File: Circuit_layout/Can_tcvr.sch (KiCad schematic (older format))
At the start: 4 parts, among them U10 MCP2551-I/SN

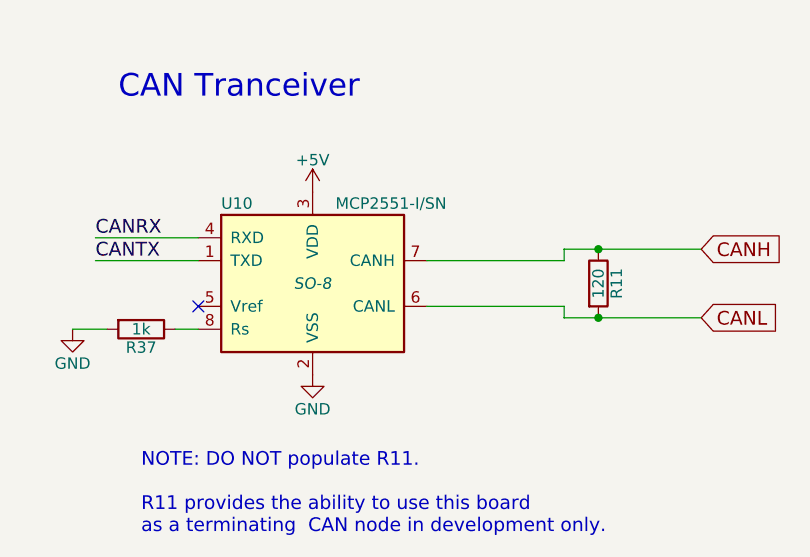
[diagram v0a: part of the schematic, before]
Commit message: Started PCB. Small changes to schematic. Adding system states visio file
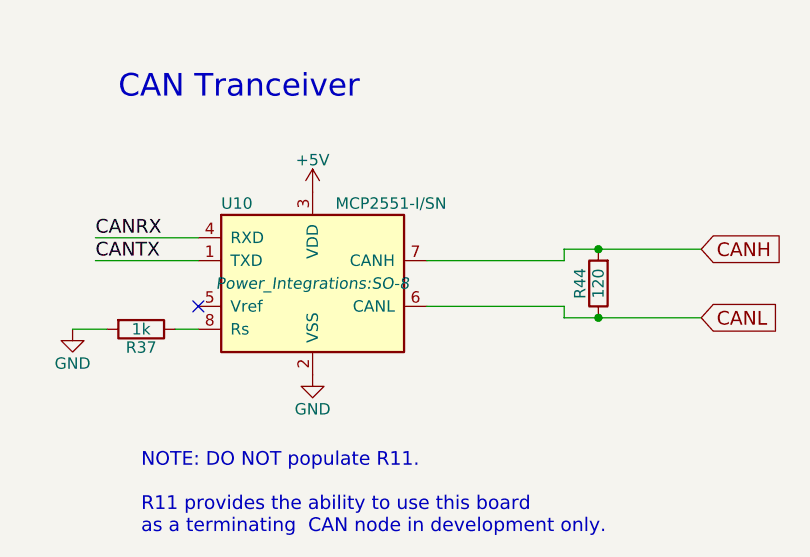
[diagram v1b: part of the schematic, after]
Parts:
- removed R11: 120, symbol R
- added R44: 120, Resistors_SMD:R_0805_HandSoldering, symbol R
- U10: footprint SO-8 -> Power_Integrations:SO-8
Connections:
- net CANH: now also R44.2
- net CANL: now also R44.1
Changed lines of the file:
@@
 F 0 "U10" H 5000 4300 50  0000 L CNN
 F 1 "MCP2551-I/SN" H 5500 4300 50  0000 L CNN
-F 2 "SO-8" H 5400 3950 50  0000 C CIN
+F 2 "Power_Integrations:SO-8" H 5400 3950 50  0000 C CIN
 F 3 "" H 5400 3950 50  0000 C CNN
 F 4 "MCP2551-I/SN-ND" H 5400 3950 60  0001 C CNN "DigiKey P/N"
@@
 Text Label 4450 3850 0    60   ~ 0
 CANTX
-$Comp
-L R R11
-U 1 1 58A633B9
-P 6650 3950
-F 0 "R11" V 6730 3950 50  0000 C CNN
-F 1 "120" V 6650 3950 50  0000 C CNN
-F 2 "" V 6580 3950 50  0000 C CNN
-F 3 "" H 6650 3950 50  0000 C CNN
-	1    6650 3950
-	1    0    0    -1
-$EndComp
 Wire Wire Line
 	5900 3850 6500 3850
@@
 CANL
 $Comp
-L GND #PWR020
+L GND #PWR021
 U 1 1 58A63637
 P 5400 4350
-F 0 "#PWR020" H 5400 4100 50  0001 C CNN
+F 0 "#PWR021" H 5400 4100 50  0001 C CNN
 F 1 "GND" H 5400 4200 50  0000 C CNN
 F 2 "" H 5400 4350 50  0000 C CNN
@@
 $EndComp
 $Comp
-L GND #PWR021
+L GND #PWR022
 U 1 1 58A6364F
 P 4350 4150
-F 0 "#PWR021" H 4350 3900 50  0001 C CNN
+F 0 "#PWR022" H 4350 3900 50  0001 C CNN
 F 1 "GND" H 4350 4000 50  0000 C CNN
 F 2 "" H 4350 4150 50  0000 C CNN
@@
 	4800 4150 4900 4150
 $Comp
-L +5V #PWR022
+L +5V #PWR023
 U 1 1 58A636CC
 P 5400 3550
-F 0 "#PWR022" H 5400 3400 50  0001 C CNN
+F 0 "#PWR023" H 5400 3400 50  0001 C CNN
 F 1 "+5V" H 5400 3690 50  0000 C CNN
 F 2 "" H 5400 3550 50  0000 C CNN
@@
 $EndComp
 $Comp
-L +5V #PWR023
+L +5V #PWR024
 U 1 1 58A636E7
 P 3800 3800
-F 0 "#PWR023" H 3800 3650 50  0001 C CNN
+F 0 "#PWR024" H 3800 3650 50  0001 C CNN
 F 1 "+5V" H 3800 3940 50  0000 C CNN
 F 2 "" H 3800 3800 50  0000 C CNN
@@
 $EndComp
 $Comp
-L GND #PWR024
+L GND #PWR025
 U 1 1 58A636FB
 P 3800 4100
-F 0 "#PWR024" H 3800 3850 50  0001 C CNN
+F 0 "#PWR025" H 3800 3850 50  0001 C CNN
 F 1 "GND" H 3800 3950 50  0000 C CNN
 F 2 "" H 3800 4100 50  0000 C CNN
@@
 	0    1    1    0
 $EndComp
+$Comp
+L R R44
+U 1 1 58BD8957
+P 6650 3950
+F 0 "R44" V 6730 3950 50  0000 C CNN
+F 1 "120" V 6650 3950 50  0000 C CNN
+F 2 "Resistors_SMD:R_0805_HandSoldering" V 6580 3950 50  0001 C CNN
+F 3 "" H 6650 3950 50  0000 C CNN
+F 4 "311-120CRCT-ND" V 6650 3950 60  0001 C CNN "DigiKey P/N"
+F 5 "http://www.digikey.com/product-detail/en/yageo/RC0805FR-07120RL/311-120CRCT-ND/730522" V 6650 3950 60  0001 C CNN "URL"
+F 6 "RC0805FR-07120RL" V 6650 3950 60  0001 C CNN "Man P/N"
+F 7 "0.1" V 6650 3950 60  0001 C CNN "Price"
+F 8 "Yageo" V 6650 3950 60  0001 C CNN "Manufacturer"
+	1    6650 3950
+	-1   0    0    1
+$EndComp
 $EndSCHEMATC

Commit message: changes before presentation
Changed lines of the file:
@@
 LIBS:xilinx
 LIBS:Zilog
+LIBS:pacman-main-cache
 LIBS:bss84
 LIBS:+10v
@@
 $Descr A4 11693 8268
 encoding utf-8
-Sheet 2 7
+Sheet 7 7
 Title "Tractive System Interface"
 Date ""
@@
 F 0 "U10" H 5000 4300 50  0000 L CNN
 F 1 "MCP2551-I/SN" H 5500 4300 50  0000 L CNN
-F 2 "Power_Integrations:SO-8" H 5400 3950 50  0000 C CIN
+F 2 "Power_Integrations:SO-8" H 5400 3950 50  0001 C CIN
 F 3 "" H 5400 3950 50  0000 C CNN
 F 4 "MCP2551-I/SN-ND" H 5400 3950 60  0001 C CNN "DigiKey P/N"
@@
 CANL
 $Comp
-L GND #PWR021
+L GND #PWR0122
 U 1 1 58A63637
 P 5400 4350
-F 0 "#PWR021" H 5400 4100 50  0001 C CNN
+F 0 "#PWR0122" H 5400 4100 50  0001 C CNN
 F 1 "GND" H 5400 4200 50  0000 C CNN
 F 2 "" H 5400 4350 50  0000 C CNN
@@
 $EndComp
 $Comp
-L GND #PWR022
+L GND #PWR0123
 U 1 1 58A6364F
 P 4350 4150
-F 0 "#PWR022" H 4350 3900 50  0001 C CNN
+F 0 "#PWR0123" H 4350 3900 50  0001 C CNN
 F 1 "GND" H 4350 4000 50  0000 C CNN
 F 2 "" H 4350 4150 50  0000 C CNN
@@
 	4800 4150 4900 4150
 $Comp
-L +5V #PWR023
+L +5V #PWR0124
 U 1 1 58A636CC
 P 5400 3550
-F 0 "#PWR023" H 5400 3400 50  0001 C CNN
+F 0 "#PWR0124" H 5400 3400 50  0001 C CNN
 F 1 "+5V" H 5400 3690 50  0000 C CNN
 F 2 "" H 5400 3550 50  0000 C CNN
@@
 $EndComp
 $Comp
-L +5V #PWR024
+L +5V #PWR0125
 U 1 1 58A636E7
 P 3800 3800
-F 0 "#PWR024" H 3800 3650 50  0001 C CNN
+F 0 "#PWR0125" H 3800 3650 50  0001 C CNN
 F 1 "+5V" H 3800 3940 50  0000 C CNN
 F 2 "" H 3800 3800 50  0000 C CNN
@@
 $EndComp
 $Comp
-L GND #PWR025
+L GND #PWR0126
 U 1 1 58A636FB
 P 3800 4100
-F 0 "#PWR025" H 3800 3850 50  0001 C CNN
+F 0 "#PWR0126" H 3800 3850 50  0001 C CNN
 F 1 "GND" H 3800 3950 50  0000 C CNN
 F 2 "" H 3800 4100 50  0000 C CNN

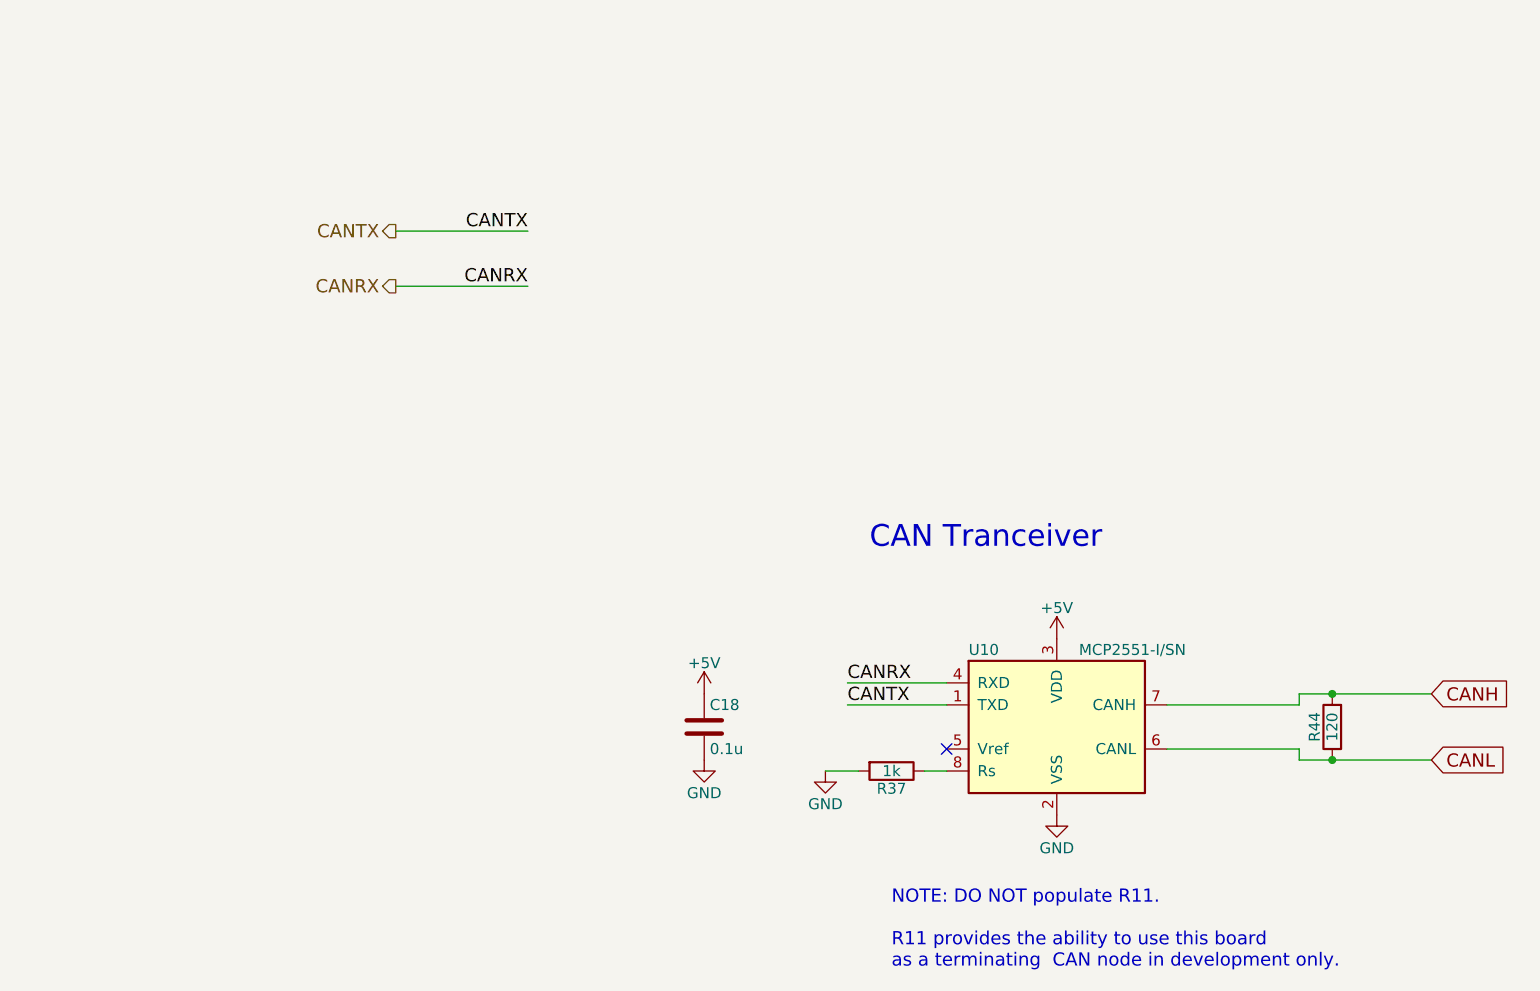
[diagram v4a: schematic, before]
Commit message: current sensor enable
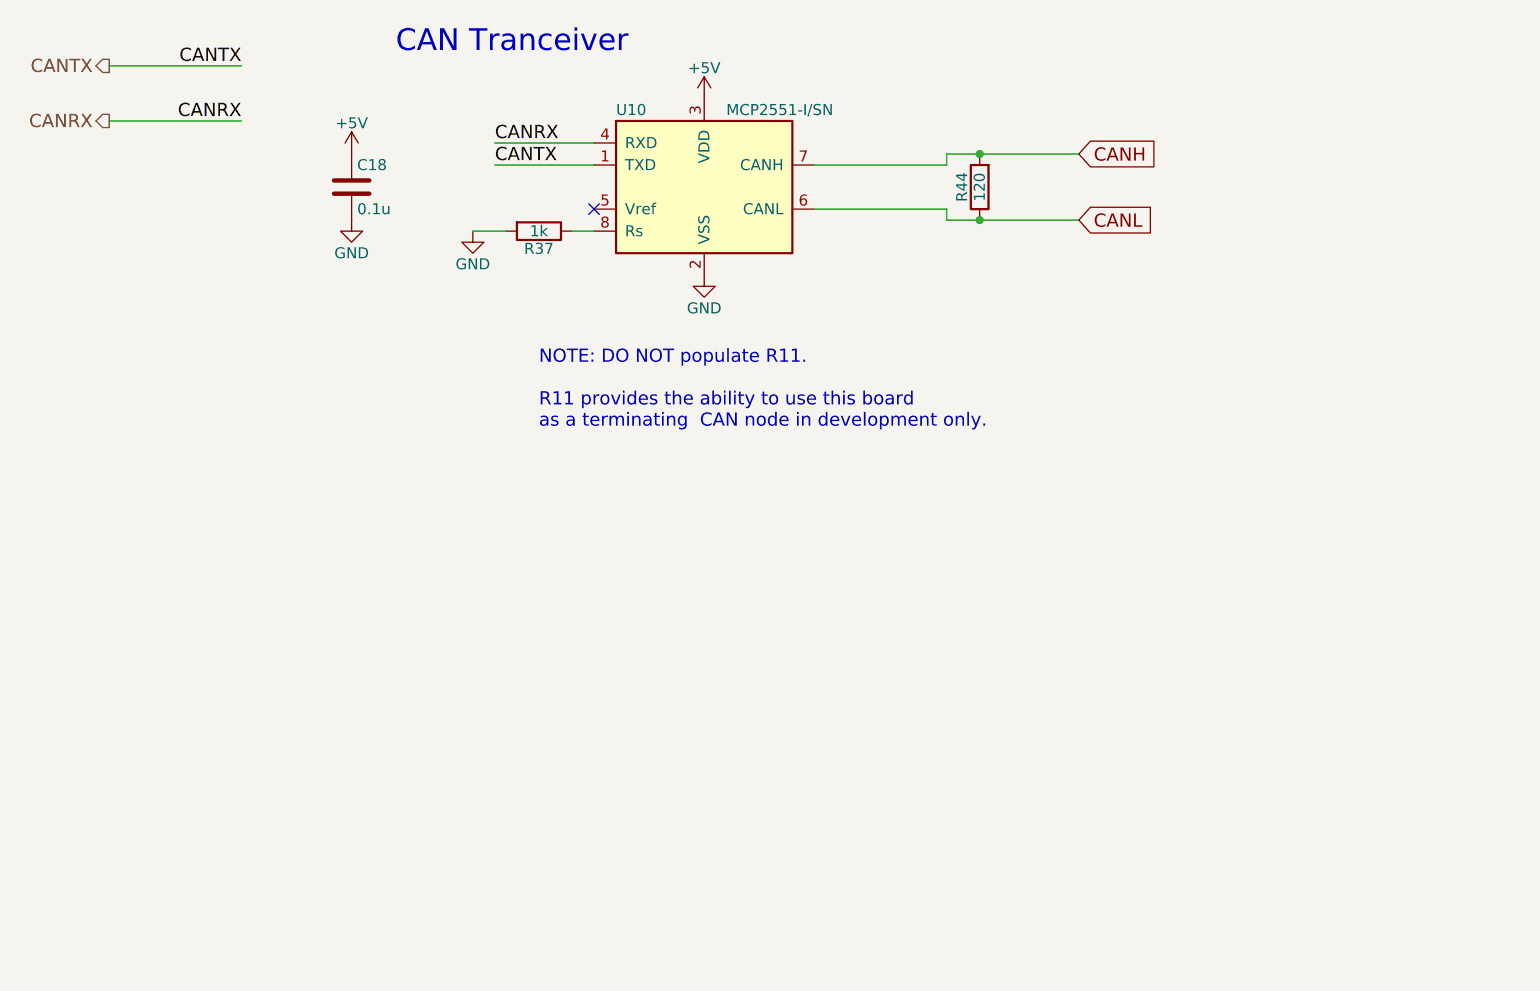
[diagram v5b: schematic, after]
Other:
- moved on the sheet: C18, R37, R44, U10
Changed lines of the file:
@@
 L MCP2551-I/SN U10
 U 1 1 58A630DD
-P 5400 3950
-F 0 "U10" H 5000 4300 50  0000 L CNN
-F 1 "MCP2551-I/SN" H 5500 4300 50  0000 L CNN
-F 2 "Power_Integrations:SO-8" H 5400 3950 50  0001 C CIN
-F 3 "" H 5400 3950 50  0000 C CNN
-F 4 "MCP2551-I/SN-ND" H 5400 3950 60  0001 C CNN "DigiKey P/N"
-F 5 "http://www.digikey.com/product-detail/en/microchip-technology/MCP2551-I-SN/MCP2551-I-SN-ND/509452" H 5400 3950 60  0001 C CNN "URL"
-	1    5400 3950
+P 3800 1500
+F 0 "U10" H 3400 1850 50  0000 L CNN
+F 1 "MCP2551-I/SN" H 3900 1850 50  0000 L CNN
+F 2 "Power_Integrations:SO-8" H 3800 1500 50  0001 C CIN
+F 3 "" H 3800 1500 50  0000 C CNN
+F 4 "MCP2551-I/SN-ND" H 3800 1500 60  0001 C CNN "DigiKey P/N"
+F 5 "http://www.digikey.com/product-detail/en/microchip-technology/MCP2551-I-SN/MCP2551-I-SN-ND/509452" H 3800 1500 60  0001 C CNN "URL"
+	1    3800 1500
 	1    0    0    -1
 $EndComp
 Wire Wire Line
-	4900 3750 4450 3750
+	3300 1300 2850 1300
 Wire Wire Line
-	4900 3850 4450 3850
-Text Label 4450 3750 0    60   ~ 0
+	3300 1400 2850 1400
+Text Label 2850 1300 0    60   ~ 0
 CANRX
-Text Label 4450 3850 0    60   ~ 0
+Text Label 2850 1400 0    60   ~ 0
 CANTX
 Wire Wire Line
-	5900 3850 6500 3850
+	4300 1400 4900 1400
 Wire Wire Line
-	6500 3850 6500 3800
+	4900 1400 4900 1350
 Wire Wire Line
-	6500 3800 7100 3800
+	4900 1350 5500 1350
 Wire Wire Line
-	5900 4050 6500 4050
+	4300 1600 4900 1600
 Wire Wire Line
-	6500 4050 6500 4100
+	4900 1600 4900 1650
 Wire Wire Line
-	6500 4100 7100 4100
-Connection ~ 6650 3800
-Connection ~ 6650 4100
-Text GLabel 7100 3800 2    60   Input ~ 0
+	4900 1650 5500 1650
+Connection ~ 5050 1350
+Connection ~ 5050 1650
+Text GLabel 5500 1350 2    60   Input ~ 0
 CANH
-Text GLabel 7100 4100 2    60   Input ~ 0
+Text GLabel 5500 1650 2    60   Input ~ 0
 CANL
 $Comp
-L GND #PWR0125
+L GND #PWR0120
 U 1 1 58A63637
-P 5400 4350
-F 0 "#PWR0125" H 5400 4100 50  0001 C CNN
-F 1 "GND" H 5400 4200 50  0000 C CNN
-F 2 "" H 5400 4350 50  0000 C CNN
-F 3 "" H 5400 4350 50  0000 C CNN
-	1    5400 4350
+P 3800 1900
+F 0 "#PWR0120" H 3800 1650 50  0001 C CNN
+F 1 "GND" H 3800 1750 50  0000 C CNN
+F 2 "" H 3800 1900 50  0000 C CNN
+F 3 "" H 3800 1900 50  0000 C CNN
+	1    3800 1900
 	1    0    0    -1
 $EndComp
 $Comp
-L GND #PWR0126
+L GND #PWR0121
 U 1 1 58A6364F
-P 4350 4150
-F 0 "#PWR0126" H 4350 3900 50  0001 C CNN
-F 1 "GND" H 4350 4000 50  0000 C CNN
-F 2 "" H 4350 4150 50  0000 C CNN
-F 3 "" H 4350 4150 50  0000 C CNN
-	1    4350 4150
+P 2750 1700
+F 0 "#PWR0121" H 2750 1450 50  0001 C CNN
+F 1 "GND" H 2750 1550 50  0000 C CNN
+F 2 "" H 2750 1700 50  0000 C CNN
+F 3 "" H 2750 1700 50  0000 C CNN
+	1    2750 1700
 	1    0    0    -1
 $EndComp
 Wire Wire Line
-	4500 4150 4350 4150
+	2900 1700 2750 1700
 Wire Wire Line
-	4800 4150 4900 4150
+	3200 1700 3300 1700
 $Comp
-L +5V #PWR0127
+L +5V #PWR0122
 U 1 1 58A636CC
-P 5400 3550
-F 0 "#PWR0127" H 5400 3400 50  0001 C CNN
-F 1 "+5V" H 5400 3690 50  0000 C CNN
-F 2 "" H 5400 3550 50  0000 C CNN
-F 3 "" H 5400 3550 50  0000 C CNN
-	1    5400 3550
+P 3800 1100
+F 0 "#PWR0122" H 3800 950 50  0001 C CNN
+F 1 "+5V" H 3800 1240 50  0000 C CNN
+F 2 "" H 3800 1100 50  0000 C CNN
+F 3 "" H 3800 1100 50  0000 C CNN
+	1    3800 1100
 	1    0    0    -1
 $EndComp
 $Comp
-L +5V #PWR0128
+L +5V #PWR0123
 U 1 1 58A636E7
-P 3800 3800
-F 0 "#PWR0128" H 3800 3650 50  0001 C CNN
-F 1 "+5V" H 3800 3940 50  0000 C CNN
-F 2 "" H 3800 3800 50  0000 C CNN
-F 3 "" H 3800 3800 50  0000 C CNN
-	1    3800 3800
+P 2200 1350
+F 0 "#PWR0123" H 2200 1200 50  0001 C CNN
+F 1 "+5V" H 2200 1490 50  0000 C CNN
+F 2 "" H 2200 1350 50  0000 C CNN
+F 3 "" H 2200 1350 50  0000 C CNN
+	1    2200 1350
 	1    0    0    -1
 $EndComp
 $Comp
-L GND #PWR0129
+L GND #PWR0124
 U 1 1 58A636FB
-P 3800 4100
-F 0 "#PWR0129" H 3800 3850 50  0001 C CNN
-F 1 "GND" H 3800 3950 50  0000 C CNN
-F 2 "" H 3800 4100 50  0000 C CNN
-F 3 "" H 3800 4100 50  0000 C CNN
-	1    3800 4100
+P 2200 1650
+F 0 "#PWR0124" H 2200 1400 50  0001 C CNN
+F 1 "GND" H 2200 1500 50  0000 C CNN
+F 2 "" H 2200 1650 50  0000 C CNN
+F 3 "" H 2200 1650 50  0000 C CNN
+	1    2200 1650
 	1    0    0    -1
 $EndComp
-NoConn ~ 4900 4050
-Text Notes 4550 3150 0    99   ~ 0
+NoConn ~ 3300 1600
+Text Notes 2400 900  0    99   ~ 0
 CAN Tranceiver
-Text HLabel 2400 1700 0    60   Output ~ 0
+Text HLabel 1100 950  0    60   Output ~ 0
 CANTX
-Text HLabel 2400 1950 0    60   Output ~ 0
+Text HLabel 1100 1200 0    60   Output ~ 0
 CANRX
 Wire Wire Line
-	2400 1700 3000 1700
+	1100 950  1700 950
 Wire Wire Line
-	2400 1950 3000 1950
-Text Label 3000 1700 2    60   ~ 0
+	1100 1200 1700 1200
+Text Label 1700 950  2    60   ~ 0
 CANTX
-Text Label 3000 1950 2    60   ~ 0
+Text Label 1700 1200 2    60   ~ 0
 CANRX
-Text Notes 4650 5050 0    60   ~ 0
+Text Notes 3050 2600 0    60   ~ 0
 NOTE: DO NOT populate R11.\n\nR11 provides the ability to use this board \nas a terminating  CAN node in development only.
 $Comp
 L C C18
 U 1 1 58B93C80
-P 3800 3950
-F 0 "C18" H 3825 4050 50  0000 L CNN
-F 1 "0.1u" H 3825 3850 50  0000 L CNN
-F 2 "Capacitors_SMD:C_0805_HandSoldering" H 3838 3800 50  0001 C CNN
-F 3 "http://www.kemet.com/Lists/ProductCatalog/Attachments/53/KEM_C1002_X7R_SMD.pdf" H 3800 3950 50  0001 C CNN
-F 4 "399-1168-1-ND" H 3800 3950 60  0001 C CNN "Digikey P/N"
-F 5 "http://www.digikey.com/product-detail/en/kemet/C0805C104K3RACTU/399-1168-1-ND/411443" H 3800 3950 60  0001 C CNN "URL"
-F 6 "C0805C104K3RACTU" H 3800 3950 60  0001 C CNN "Man P/N"
-	1    3800 3950
+P 2200 1500
+F 0 "C18" H 2225 1600 50  0000 L CNN
+F 1 "0.1u" H 2225 1400 50  0000 L CNN
+F 2 "Capacitors_SMD:C_0805_HandSoldering" H 2238 1350 50  0001 C CNN
+F 3 "http://www.kemet.com/Lists/ProductCatalog/Attachments/53/KEM_C1002_X7R_SMD.pdf" H 2200 1500 50  0001 C CNN
+F 4 "399-1168-1-ND" H 2200 1500 60  0001 C CNN "Digikey P/N"
+F 5 "http://www.digikey.com/product-detail/en/kemet/C0805C104K3RACTU/399-1168-1-ND/411443" H 2200 1500 60  0001 C CNN "URL"
+F 6 "C0805C104K3RACTU" H 2200 1500 60  0001 C CNN "Man P/N"
+	1    2200 1500
 	1    0    0    -1
 $EndComp
@@
 L R R37
 U 1 1 58B983FD
-P 4650 4150
-F 0 "R37" V 4730 4150 50  0000 C CNN
-F 1 "1k" V 4650 4150 50  0000 C CNN
-F 2 "Resistors_SMD:R_0805_HandSoldering" V 4580 4150 50  0001 C CNN
-F 3 "" H 4650 4150 50  0000 C CNN
-F 4 "P1.00KCCT-ND" V 4650 4150 60  0001 C CNN "DigiKey P/N"
-F 5 "http://www.digikey.com/product-detail/en/panasonic-electronic-components/ERJ-6ENF1001V/P1.00KCCT-ND/118957" V 4650 4150 60  0001 C CNN "URL"
-F 6 "ERJ-6ENF1001V" V 4650 4150 60  0001 C CNN "Man P/N"
-	1    4650 4150
+P 3050 1700
+F 0 "R37" V 3130 1700 50  0000 C CNN
+F 1 "1k" V 3050 1700 50  0000 C CNN
+F 2 "Resistors_SMD:R_0805_HandSoldering" V 2980 1700 50  0001 C CNN
+F 3 "" H 3050 1700 50  0000 C CNN
+F 4 "P1.00KCCT-ND" V 3050 1700 60  0001 C CNN "DigiKey P/N"
+F 5 "http://www.digikey.com/product-detail/en/panasonic-electronic-components/ERJ-6ENF1001V/P1.00KCCT-ND/118957" V 3050 1700 60  0001 C CNN "URL"
+F 6 "ERJ-6ENF1001V" V 3050 1700 60  0001 C CNN "Man P/N"
+	1    3050 1700
 	0    1    1    0
 $EndComp
@@
 L R R44
 U 1 1 58BD8957
-P 6650 3950
-F 0 "R44" V 6730 3950 50  0000 C CNN
-F 1 "120" V 6650 3950 50  0000 C CNN
-F 2 "Resistors_SMD:R_0805_HandSoldering" V 6580 3950 50  0001 C CNN
-F 3 "" H 6650 3950 50  0000 C CNN
-F 4 "311-120CRCT-ND" V 6650 3950 60  0001 C CNN "DigiKey P/N"
-F 5 "http://www.digikey.com/product-detail/en/yageo/RC0805FR-07120RL/311-120CRCT-ND/730522" V 6650 3950 60  0001 C CNN "URL"
-F 6 "RC0805FR-07120RL" V 6650 3950 60  0001 C CNN "Man P/N"
-F 7 "0.1" V 6650 3950 60  0001 C CNN "Price"
-F 8 "Yageo" V 6650 3950 60  0001 C CNN "Manufacturer"
-	1    6650 3950
+P 5050 1500
+F 0 "R44" V 5130 1500 50  0000 C CNN
+F 1 "120" V 5050 1500 50  0000 C CNN
+F 2 "Resistors_SMD:R_0805_HandSoldering" V 4980 1500 50  0001 C CNN
+F 3 "" H 5050 1500 50  0000 C CNN
+F 4 "311-120CRCT-ND" V 5050 1500 60  0001 C CNN "DigiKey P/N"
+F 5 "http://www.digikey.com/product-detail/en/yageo/RC0805FR-07120RL/311-120CRCT-ND/730522" V 5050 1500 60  0001 C CNN "URL"
+F 6 "RC0805FR-07120RL" V 5050 1500 60  0001 C CNN "Man P/N"
+F 7 "0.1" V 5050 1500 60  0001 C CNN "Price"
+F 8 "Yageo" V 5050 1500 60  0001 C CNN "Manufacturer"
+	1    5050 1500
 	-1   0    0    1
 $EndComp
